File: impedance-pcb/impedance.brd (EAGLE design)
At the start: 38.1 x 36.8 mm, 26 parts, among them U3 ADG704BRMZ, U4 ADG787BRMZ, U5 RED

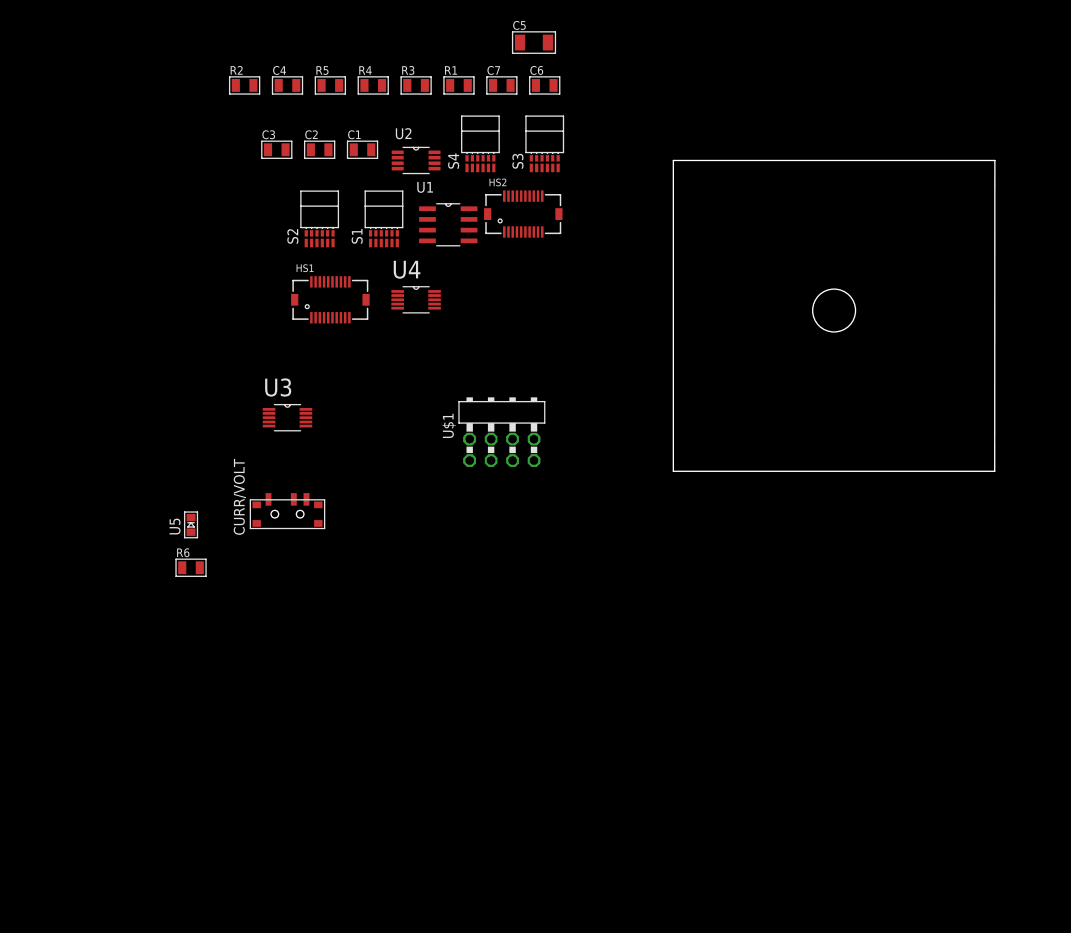
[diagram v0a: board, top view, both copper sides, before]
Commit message: Created plating/impedance testing circuit. Need to get parts to prototype it.
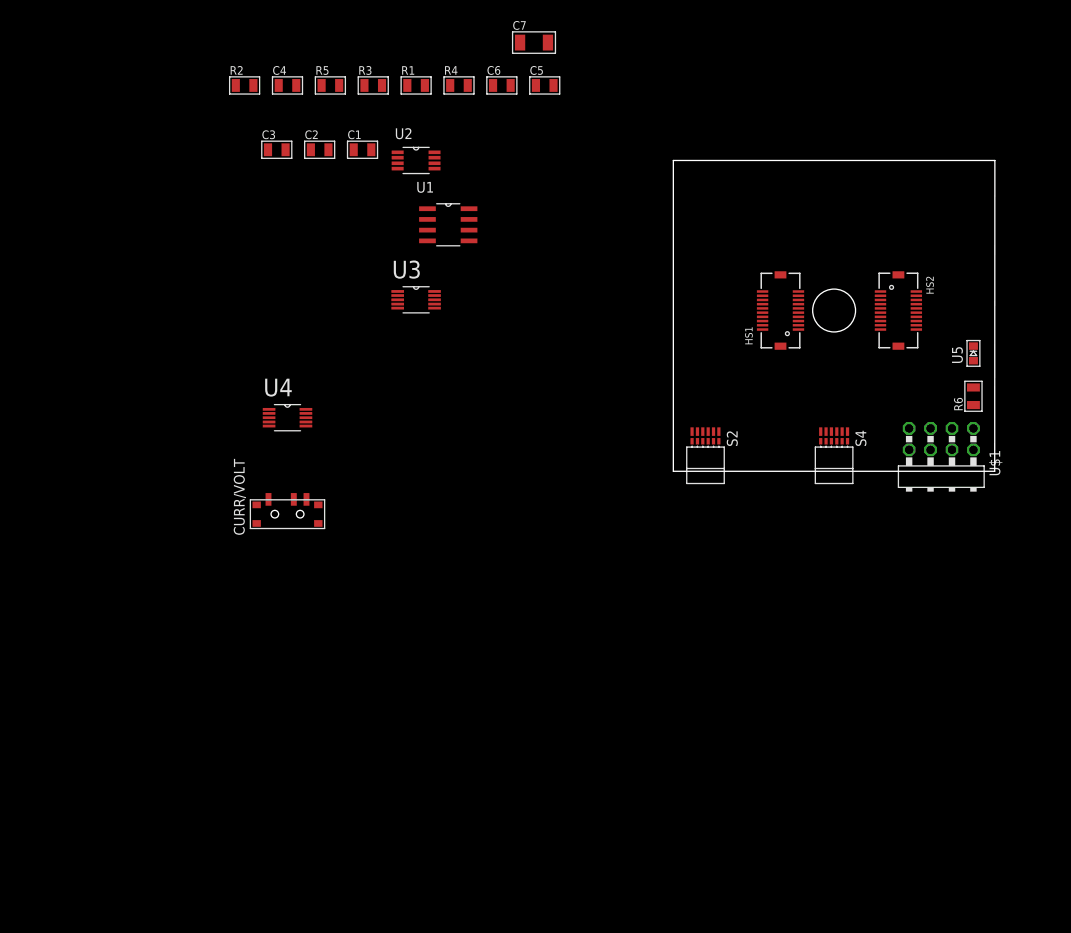
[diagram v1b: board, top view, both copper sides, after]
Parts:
- removed S1, S3: RHD2000-CABLE-AMP-SIDE, RHD2000:OMNETICS_PZN-12-AA
- C5: value (none) -> 0.1uF; device impedance:1206 -> impedance:0805
- C7: value 0.1uF -> (none); device impedance:0805 -> impedance:1206
- R1: value 40.2k -> 100k
- R4: value 100k -> 40.2k
- U3: value ADG704BRMZ -> ADG787BRMZ
- U4: value ADG787BRMZ -> ADG704BRMZ
- moved R6 94.9 mm to (35.6, 8.89), turned to 90 degrees
- moved U5 94.9 mm to (35.6, 14.0)
- moved S4 55.0 mm to (19.1, 2.54), turned to 180 degrees
- moved HS1 53.4 mm to (12.7, 19.1), turned to 90 degrees
- moved S2 52.9 mm to (3.81, 2.54), turned to 180 degrees
- moved U$1 52.1 mm to (31.8, 2.54), turned to 180 degrees
- moved HS2 45.9 mm to (26.7, 19.1), turned to 270 degrees
- moved U3 20.7 mm to (-30.5, 20.3)
- moved U4 20.7 mm to (-45.7, 6.35)
- moved R4 10.2 mm to (-25.4, 45.7)
- moved C7 6.35 mm to (-16.5, 50.8)
- moved C5 5.24 mm to (-15.2, 45.7)
- moved R1 5.08 mm to (-30.5, 45.7)
- moved R3 5.08 mm to (-35.6, 45.7)
- moved C6 5.08 mm to (-20.3, 45.7)
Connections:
- removed net MIS02-2: HS2.9, S4.B4
- removed net MISO1+3: HS2.8, S3.T4
- new net MISO1+2: HS2.8, S4.T4
- new net MISO2-2: HS2.9, S4.B5
- net +3.3V: now also C7.1, S4.T6; no longer C5.1, S3.T6
- net +3.3V1: now also C5.1, U3.1; no longer C6.1, U4.1
- net +3.3V2: now also C6.1, U4.6; no longer C7.1, U3.6
- net AGND: now also S4.B6, U3.10, U3.5, U3.6, U4.3; no longer S3.B6, U3.3, U4.10, U4.5, U4.6
- net BATH: now also U$1.4, U3.9; no longer U4.9
- net BATH_POLARITY: now also U3.4, U3.8; no longer U4.4, U4.8
- net CS+1: no longer S1.T1
- net CS+2: no longer S3.T1
- net CS-1: no longer S1.B1
- net CS-2: no longer S3.B1
- net ELEC_TEST: now also U3.3; no longer U4.3
- net ELEC_TEST_A1: now also U4.2; no longer U3.2
- net ELEC_TEST_A2: now also U4.9; no longer U3.9
- net ELEC_TEST_B1: now also U4.4; no longer U3.4
- net ELEC_TEST_B2: now also U4.7; no longer U3.7
- net GND: no longer S1.B6, S4.B6
- net IOUT: now also U3.2, U3.7; no longer U4.2, U4.7
- net MIS02-1: now also S2.B5; no longer S1.B4
- net MISO1-2: now also S4.B4; no longer S3.B4
- net MISO2+1: now also S2.T5; no longer S1.T4
- net MISO2+2: now also S4.T5; no longer S4.T4
- net MOSI+1: no longer S1.T3
- net MOSI+2: no longer S3.T3
- net MOSI-1: no longer S1.B3
- net MOSI-2: no longer S3.B3
- net N$1: now also R1.2; no longer R3.2
- net N$2: now also R4.2; no longer R1.2
- net N$3: now also R4.1; no longer R1.1
- net N$4: now also R1.1; no longer R3.1
- net N$5: now also R3.1; no longer R4.1
- net N$6: now also R3.2; no longer R4.2
- net N$8: now also U4.8; no longer U3.8
- net PLATE: now also U4.5; no longer U3.5
- net RHD_SEL_A: now also U4.1; no longer U3.1
- net RHD_SEL_B: now also U4.10; no longer U3.10
- net SCLK+1: no longer S1.T2
- net SCLK+2: no longer S3.T2
- net SCLK-1: no longer S1.B2
- net SCLK-2: no longer S3.B2

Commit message: Updated the impedance test interface schematic based on testing.
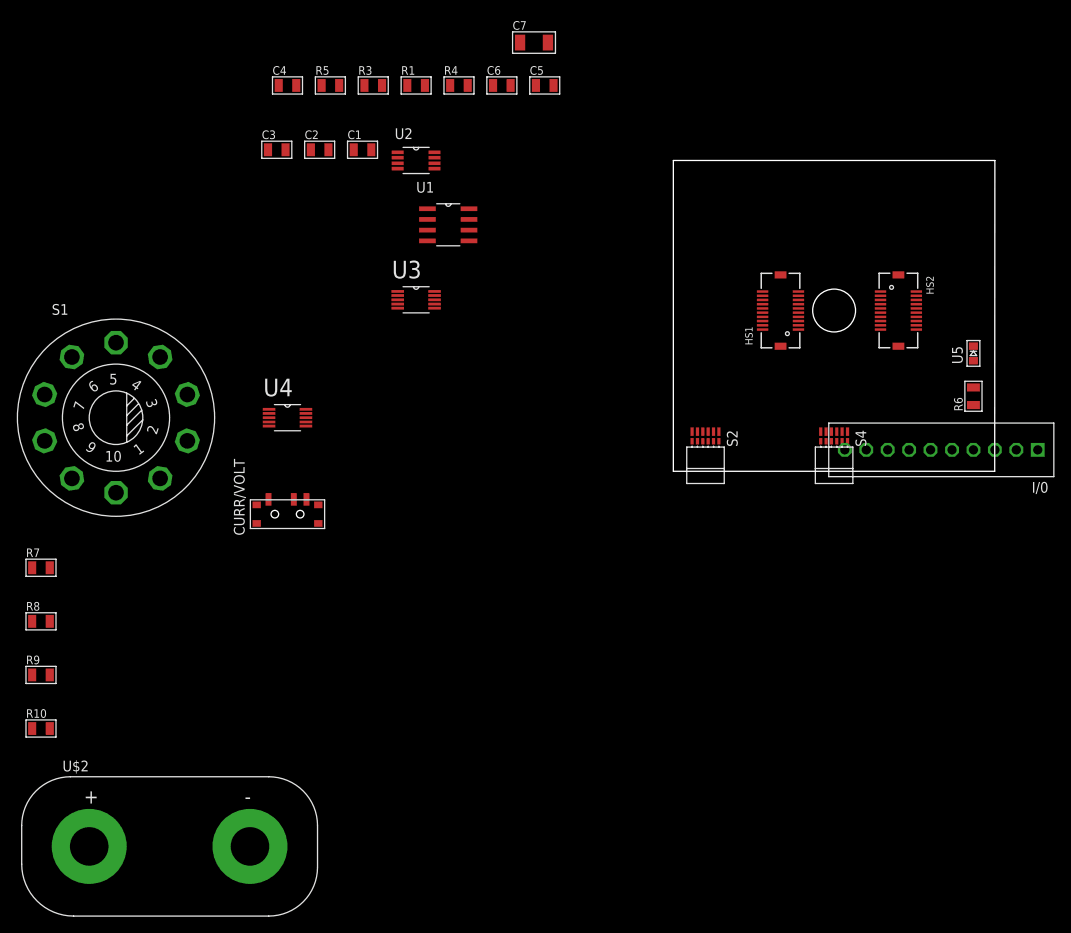
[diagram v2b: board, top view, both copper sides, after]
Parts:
- removed R2: 1M, impedance:0805
- removed U$1: PINHD-2X4, impedance:2X04/90
- added I/0: SCREW10_0.1-THRU, impedance:SCREW10
- added R10: 3.3k, impedance:0805
- added R7: 3.3M, impedance:0805
- added R8: 330k, impedance:0805
- added R9: 33k, impedance:0805
- added S1: RSER, impedance:R-SWITCH
- added U$2: DUAL-POST_BANANA, impedance:BANANA-BINDING-POST
- C1: value 0.1uF -> 10nF
- C7: value (none) -> 10uF
- U1: value (none) -> OPA333
- U2: value (none) -> INA326
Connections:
- removed net +3.3V1: C5.1, U3.1
- removed net +3.3V2: C6.1, U4.6
- removed net N$8: CURR/VOLT.2, U4.8
- new net N$10: CURR/VOLT.1, R10.1, R7.1, R8.1, R9.1, U2.2
- new net N$11: R10.2, S1.4
- new net N$12: R9.2, S1.3
- new net N$13: R8.2, S1.2
- new net N$14: R7.2, S1.1
- new net N$15: U$2.-, U3.9
- net +3.3V: now also C5.1, C6.1, I/0.P$2, U3.1, U4.6; no longer CURR/VOLT.3
- net AGND: now also I/0.P$10, I/0.P$3, I/0.P$9; no longer U$1.3
- net BATH: now also I/0.P$4, U$2.+; no longer U$1.4, U3.9
- net BATH_POLARITY: now also I/0.P$5; no longer U$1.5
- net ELEC_TEST: now also U4.8; no longer CURR/VOLT.1
- net IOUT: now also CURR/VOLT.2; no longer R2.1, U2.2
- net N$1: now also S1.10; no longer R2.2
- net PLATE: now also I/0.P$6; no longer U$1.6
- net RHD_SEL_A: now also I/0.P$7; no longer U$1.7
- net RHD_SEL_B: now also I/0.P$8; no longer U$1.8
- net VIN: now also CURR/VOLT.3, I/0.P$1; no longer U$1.1
